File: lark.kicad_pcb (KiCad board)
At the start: 2 copper layers, 113 parts, among them CON1 SJ1-3523N, IC1 MS5611-01BA03, IC2 MS5611-01BA03, J1 SPI, J2 UART0, J3 I2C_0, J4 PWR_IN, J7 54602-908LF, J8 54602-908LF, J9 SOUND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

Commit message: Fitting layout into 57 mm instrument.
* board width is 51 mm at the moment
* split into two boards (sensor and main) which can be stacked with
  2.54 mm pinheaders.
* ESP32 was put to bottom with optional pcb antenna facing to front.
* added footprint for optional HCLAxxE on sensorboard
* added footprint for BMI088

* Is multiple GND pins for sensor board really a good idea (ground loops)?
* Does the +12V topology make sense (especially regarding the external
  IGC ports)?
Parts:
- removed C33, C34: 100n, Capacitor_SMD:C_0805_2012Metric_Pad1.15x1.40mm_HandSolder
- removed D3: 50V/3A, Diode_SMD:D_SOD-123
- removed L4: Ferrite_Bead, Inductor_SMD:L_0805_2012Metric_Pad1.15x1.40mm_HandSolder
- removed RV1: 3A/24V, Fuse:Fuse_2920_7451Metric_Pad2.10x5.45mm_HandSolder
- removed U8: BMX055, BMX055:BMX055
- added C25: 100n, Capacitor_SMD:C_0805_2012Metric_Pad1.15x1.40mm_HandSolder, F.Cu at (131.9, -34.1)
- added C26: 100n, Capacitor_SMD:C_0805_2012Metric_Pad1.15x1.40mm_HandSolder, F.Cu at (131.9, -36.0)
- added F3: 1.25A/16V, Fuse:Fuse_1812_4532Metric_Pad1.30x3.40mm_HandSolder, F.Cu at (36.0, 84.0)
- added J10: Conn_01x05-Connector_Generic, Connector_PinHeader_2.54mm:PinHeader_1x05_P2.54mm_Vertical, F.Cu at (-20.0, 94.0)
- added J11: Conn_01x20, Connector_PinSocket_2.54mm:PinSocket_1x20_P2.54mm_Vertical, F.Cu at (43.0, 52.0)
- added J12: Conn_01x20, Connector_PinSocket_2.54mm:PinSocket_1x20_P2.54mm_Vertical, F.Cu at (43.0, 97.0)
- added J5: Conn_01x05-Connector_Generic, Connector_PinHeader_2.54mm:PinHeader_1x05_P2.54mm_Vertical, F.Cu at (11.0, 52.0)
- added J6: Conn_01x05-Connector_Generic, Connector_PinHeader_2.54mm:PinHeader_1x05_P2.54mm_Vertical, F.Cu at (11.0, 97.0)
- added L3: Ferrite_Bead, Inductor_SMD:L_0805_2012Metric_Pad1.15x1.40mm_HandSolder, F.Cu at (-16.6, 104.4)
- added U6: BMI088, libs:LGA-16_handsolder, F.Cu at (84.0, 86.0)
- added U7: HCLAxxE, libs:HCLAxxE, F.Cu at (11.5, 90.5)
- C12, C9: value 1u -> 10u
- D4, D5: footprint Diode_SMD:D_SOD-123 -> Diode_SMD:D_SMA_Handsoldering
- F1: value 1.25A/16V -> 3A/24V
- L1: value 6A max. -> 10uH; footprint Inductor_SMD:L_1206_3216Metric_Pad1.42x1.75mm_HandSolder -> Inductor_SMD:L_Wuerth_WE-PD2-Typ-L
- MOD1: moved to B.Cu
- moved R26 226.6 mm to (10.5, 73.0), turned to 180 degrees
- moved R25 222.2 mm to (10.5, 60.5), turned to 180 degrees
- moved C23 190.2 mm to (-19.2, 104.6), turned to 270 degrees
- moved C22 181.6 mm to (-13.2, 104.6), turned to 270 degrees
- moved R38 176.9 mm to (10.5, 70.5), turned to 180 degrees
- moved R37 176.6 mm to (10.5, 63.0), turned to 180 degrees
- moved U4 176.0 mm to (-9.24, 104.6), turned to 270 degrees
- moved C21 169.4 mm to (-4.24, 104.6), turned to 270 degrees
- moved U5 146.6 mm to (1.00, 66.0), turned to 0 degrees
- moved C24 134.2 mm to (4.53, 57.0), turned to 0 degrees
- moved R17 107.2 mm to (10.5, 55.5), turned to 180 degrees
- moved R16 100.3 mm to (10.5, 68.0), turned to 180 degrees
- moved C36 96.8 mm to (-17.0, 71.0), turned to 0 degrees
- moved C16 96.3 mm to (54.0, 76.0), turned to 90 degrees
- moved C35 91.3 mm to (-16.5, 55.0), turned to 0 degrees
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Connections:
- net /Power/SENSPWR renamed /Sensors/SENSPWR
- net Net-(IC1-Pad7) renamed /Sensors/SDA0
- net Net-(IC1-Pad8) renamed /Sensors/SCK0
- net Net-(IC2-Pad7) renamed /Sensors/SDA1
- net Net-(IC2-Pad8) renamed /Sensors/SCK1
- net Net-(R26-Pad2) renamed /Sensors/SDA2
- net Net-(R38-Pad2) renamed /Sensors/SCK2
- C11 pad 1: +12V -> /Power/PWRIN
- C12 pad 1: +12V -> /Power/PWRIN
- C8 pad 1: Net-(C8-Pad1) -> +12V
- C9 pad 1: Net-(C8-Pad1) -> +12V
- D4 pad 1: Net-(D3-Pad2) -> +12V
- D5 pad 1: +12V -> /Power/PWRIN
- F1 pad 1: Net-(F1-Pad1) -> +12V
- F1 pad 2: +12V -> Net-(F1-Pad2)
- J4 pad 1: Net-(J4-Pad1) -> Net-(F1-Pad2)
- J7 pad 7: Net-(F1-Pad1) -> Net-(F2-Pad1)
- J7 pad 8: Net-(F1-Pad1) -> Net-(F2-Pad1)
- J8 pad 7: Net-(F2-Pad1) -> Net-(F3-Pad1)
- J8 pad 8: Net-(F2-Pad1) -> Net-(F3-Pad1)
- L1 pad 2: Net-(C8-Pad1) -> /Power/PWRIN
- R16 pad 2: Net-(R16-Pad2) -> /Sensors/SDA3
- R22 pad 1: +12V -> /Power/PWRIN
- R29 pad 2: Net-(R29-Pad2) -> /Sensors/SCK3
- U2 pad 1: +12V -> /Power/PWRIN
- U5 pad 15: Net-(R29-Pad2) -> /Sensors/SDA3
- U5 pad 16: Net-(R16-Pad2) -> /Sensors/SCK3
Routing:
- net /Sensors/SDA2: track 0.00 -> 46.5 mm, vias 0 -> 2
- net I2C0_SCK: track 44.7 -> 0.00 mm
- net I2C0_SDA: track 43.8 -> 0.00 mm
- net /Sensors/SCK2: track 0.00 -> 40.1 mm
- net SPID: track 8.72 -> 36.9 mm, vias 0 -> 1
- net Net-(R27-Pad1): track 0.00 -> 27.4 mm
- net Net-(R28-Pad1): track 0.00 -> 27.0 mm
- net /Sensors/SCK0: track 0.00 -> 26.7 mm, vias 0 -> 1
- net SPIQ: track 7.39 -> 33.7 mm, vias 0 -> 1
- net /Sensors/SDA0: track 0.00 -> 25.6 mm, vias 0 -> 1
- net /Sensors/SCK1: track 0.00 -> 25.4 mm, vias 0 -> 2
- net /Sensors/SDA1: track 0.00 -> 24.4 mm, vias 0 -> 2
- net SPICLK: track 7.14 -> 29.3 mm, vias 0 -> 1
- net BOOTM: track 15.1 -> 0.00 mm, vias 1 -> 0
- net SPICS0: track 14.2 -> 0.00 mm, vias 1 -> 0
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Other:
- board outline added: 150 x 51 mm

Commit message: Layout almost complete.
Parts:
- removed C26, C5, C6: 100n, Capacitor_SMD:C_0805_2012Metric_Pad1.15x1.40mm_HandSolder
- removed J12: Conn_01x20, Connector_PinSocket_2.54mm:PinSocket_1x20_P2.54mm_Vertical
- removed R10, R11, R12, R3, R4, R5, R6, R9: 10k, Resistor_SMD:R_0805_2012Metric_Pad1.15x1.40mm_HandSolder
- removed SW1: SW_ENTR, Button_Switch_THT:SW_Tactile_SPST_Angled_PTS645Vx83-2LFS
- removed SW2: SW_UP, Button_Switch_THT:SW_Tactile_SPST_Angled_PTS645Vx83-2LFS
- removed SW3: SW_DOWN, Button_Switch_THT:SW_Tactile_SPST_Angled_PTS645Vx83-2LFS
- removed SW4: SW_VARIO, TerminalBlock_Phoenix:TerminalBlock_Phoenix_PT-1,5-2-3.5-H_1x02_P3.50mm_Horizontal
- added H1: MountingHole, MountingHole:MountingHole_3.2mm_M3_DIN965, F.Cu at (191.4, 89.0)
- added H2: MountingHole, MountingHole:MountingHole_3.2mm_M3_DIN965, F.Cu at (141.4, 89.0)
- added H3: MountingHole, MountingHole:MountingHole_3.2mm_M3_DIN965, F.Cu at (191.4, 134.0)
- added H4: MountingHole, MountingHole:MountingHole_3.2mm_M3_DIN965, F.Cu at (141.4, 134.0)
- added IC3: BMP388, libs:LGA-10_2.0x2.0x0.75_handsolder, B.Cu at (68.6, 96.4)
- added IC4: BMP388, libs:LGA-10_2.0x2.0x0.75_handsolder, B.Cu at (68.6, 111.7)
- added TP1: dummy-mounting-footprint, libs:lark_sensor_mount, F.Cu at (67.4, 89.0)
- C3, C4: footprint Capacitor_SMD:C_0805_2012Metric_Pad1.15x1.40mm_HandSolder -> Capacitor_SMD:C_0603_1608Metric; moved to B.Cu
- J1: value SPI -> CONN1; footprint Connector_PinHeader_2.54mm:PinHeader_1x07_P2.54mm_Vertical -> Connector_PinHeader_2.54mm:PinHeader_1x15_P2.54mm_Vertical
- J11: value Conn_01x20 -> CONN1; footprint Connector_PinSocket_2.54mm:PinSocket_1x20_P2.54mm_Vertical -> Connector_PinHeader_2.54mm:PinHeader_1x15_P2.54mm_Vertical
- J2: value UART0 -> Conn_01x05-Connector_Generic; footprint Connector_PinHeader_2.54mm:PinHeader_1x06_P2.54mm_Vertical -> Connector_PinHeader_2.54mm:PinHeader_1x05_P2.54mm_Vertical
- J3: value I2C_0 -> Conn_01x05-Connector_Generic; footprint Connector_PinHeader_2.54mm:PinHeader_1x04_P2.54mm_Vertical -> Connector_PinHeader_2.54mm:PinHeader_1x05_P2.54mm_Vertical
- MOD1: moved to F.Cu
- moved C25 165.3 mm to (176.9, 125.0), turned to 90 degrees
- moved J11 164.3 mm to (185.4, 134.0), turned to 270 degrees
- moved C18 156.6 mm to (169.9, 129.5), turned to 270 degrees
- moved U3 156.1 mm to (173.9, 129.5), turned to 180 degrees
- moved C19 155.8 mm to (176.9, 129.5), turned to 270 degrees
- moved C20 148.3 mm to (174.4, 125.0)
- moved L2 147.6 mm to (171.9, 125.0), turned to 270 degrees
- moved C4 147.2 mm to (65.5, 111.7)
- moved J2 145.6 mm to (81.9, 134.0), turned to 90 degrees
- moved U1 145.5 mm to (158.2, 95.2), turned to 0 degrees
- moved C3 145.5 mm to (65.5, 96.4)
- moved C13 144.5 mm to (157.9, 92.5), turned to 0 degrees
- moved C15 143.3 mm to (162.7, 94.8), turned to 0 degrees
- moved C14 143.0 mm to (162.7, 92.5), turned to 0 degrees
- moved J1 123.5 mm to (185.4, 89.0), turned to 270 degrees
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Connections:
- C3 pad 1: BUT_ENTR -> GND
- C3 pad 2: GND -> /Sensors/SENSPWR
- C4 pad 1: BUT_UP -> GND
- C4 pad 2: GND -> /Sensors/SENSPWR
- J1 pad 1: +5V -> GND
- J1 pad 3: SPICLK -> +5V
- J1 pad 4: SPIQ -> BUT_ENTR
- J1 pad 5: SPID -> BUT_UP
- J1 pad 6: SPICS0 -> BUT_DOWN
- J1 pad 7: GND -> SW_VARIO
- J11 pad 1: Net-(J11-Pad1) -> GND
- J11 pad 11: Net-(J11-Pad11) -> EN
- J11 pad 12: Net-(J11-Pad12) -> BOOTM
- J11 pad 13: Net-(J11-Pad13) -> GND
- J11 pad 14: BUT_ENTR -> Net-(J11-Pad14)
- J11 pad 15: BUT_UP -> Net-(J11-Pad15)
- J11 pad 2: Net-(J11-Pad2) -> VDD
- J11 pad 3: Net-(J11-Pad3) -> +5V
- J11 pad 4: Net-(J11-Pad4) -> SPID
- J11 pad 5: Net-(J11-Pad5) -> SPIQ
- J11 pad 6: Net-(J11-Pad6) -> SPICLK
- J11 pad 7: Net-(J11-Pad7) -> SPICS0
- J11 pad 8: Net-(J11-Pad8) -> VDD
- J11 pad 9: Net-(J11-Pad9) -> U0RXD
- J2 pad 1: VDD -> +5V
- J2 pad 2: U0RXD -> Net-(J2-Pad2)
- J2 pad 3: Net-(J2-Pad3) -> I2C0_SDA
- J2 pad 4: EN -> I2C0_SCK
- J2 pad 5: BOOTM -> GND
- J3 pad 1: VDD -> +5V
- J3 pad 2: I2C0_SCK -> Net-(J3-Pad2)
- J3 pad 4: GND -> I2C0_SCK
- J5 pad 1: GND -> +5V
- J5 pad 2: I2C0_SCK -> Net-(J5-Pad2)
- J5 pad 4: Net-(J5-Pad4) -> I2C0_SCK
- J6 pad 1: +5V -> Net-(J6-Pad1)
- J6 pad 5: GND -> Net-(J6-Pad5)
- R23 pad 1: Net-(J2-Pad3) -> Net-(J11-Pad10)
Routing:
- net +5V: track 0.00 -> 259.5 mm, vias 0 -> 2
- net /Sensors/SENSPWR: track 4.37 -> 216.0 mm, vias 0 -> 2
- net VDD: track 0.00 -> 135.1 mm, vias 0 -> 5
- net I2C0_SCK: track 0.00 -> 134.4 mm, vias 0 -> 2
- net I2C0_SDA: track 0.00 -> 130.7 mm, vias 0 -> 2
- net Net-(J7-Pad3): track 0.00 -> 49.9 mm, vias 0 -> 2
- net EN: track 0.00 -> 49.4 mm, vias 0 -> 1
- net Net-(J8-Pad3): track 0.00 -> 49.0 mm, vias 0 -> 2
- net Net-(J8-Pad4): track 0.00 -> 47.1 mm, vias 0 -> 2
- net Net-(J7-Pad4): track 0.00 -> 41.1 mm, vias 0 -> 2
- net +12V: track 0.00 -> 38.1 mm
- net /Power/PWRIN: track 0.00 -> 33.3 mm
- net SW_VARIO: track 0.00 -> 32.9 mm, vias 0 -> 1
- net /Sensors/SCK3: track 6.21 -> 37.3 mm
- net BOOTM: track 0.00 -> 30.6 mm, vias 0 -> 2
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- added copper zone on B.Cu, net GND
- added copper zone on F.Cu, net GND
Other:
- board size 150 x 51 mm -> 137.5 x 51 mm
- net class Power2 removed

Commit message: even more finished
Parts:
- moved C1 46.8 mm to (157.4, 130.0)
- moved R2 44.5 mm to (159.4, 130.0)
- moved CON1 3.19 mm to (109.4, 128.5)
- moved J9 3.00 mm to (114.9, 133.0)
- moved C39 0.62 mm to (153.9, 128.0)
- moved F3 0.50 mm to (119.7, 104.0)
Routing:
- net EN: track 49.4 -> 54.6 mm
- net SPIQ: track 33.2 -> 36.9 mm
- net Net-(J9-Pad4): track 9.68 -> 13.3 mm
- net Net-(J9-Pad3): track 13.9 -> 17.5 mm
- net Net-(CON1-Pad1): track 25.4 -> 28.8 mm
- net Net-(CON1-Pad2): track 17.1 -> 19.9 mm
- net Net-(D2-Pad2): track 0.00 -> 1.95 mm
- net Net-(D1-Pad2): track 0.00 -> 1.95 mm
- net INT_ACC: track 36.7 -> 38.4 mm
- net VDD: track 135.1 -> 136.3 mm
- net SND_R: track 23.4 -> 24.3 mm
- net SND_L: track 27.6 -> 26.9 mm
- net I2C0_SCK: track 134.4 -> 133.8 mm
- net BUT_DOWN: track 16.5 -> 16.0 mm
- net GND: track 22.5 -> 22.9 mm, vias 33 -> 91
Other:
- outline, holes or cut-outs redrawn
- board text added: "+"
- board text added: "3V3"
- board text added: "5V"
- board text added: "BOOTM"
- board text added: "CLK"
- board text added: "CS0"
- board text added: "EN"
- board text added: "GND"
- board text added: "LED1"
- board text added: "LED2"
- board text added: "Lark Baro 2019-03.1"
- board text added: "Lark ESP32 2019-03.1"
- board text added: "Lark Vario"
- board text added: "MISO"
- board text added: "MOSI"
- board text added: "NC"
- board text added: "RX"
- board text added: "SCK"
- board text added: "SDA"
- board text added: "SW1"
- board text added: "SW2"
- board text added: "SW3"
- board text added: "SW4"
- board text added: "TX"

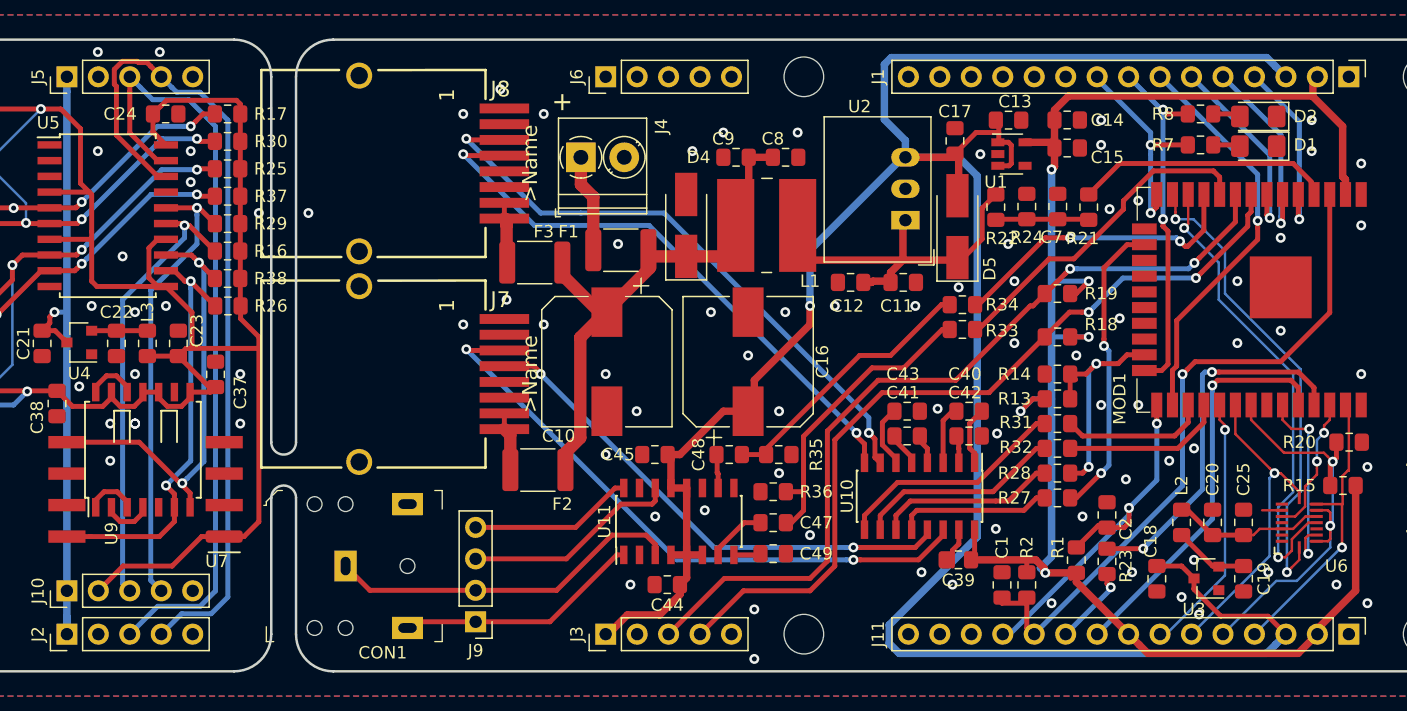
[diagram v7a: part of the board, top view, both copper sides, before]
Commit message: fix some vias
they were not shown correctly in the preview on aisler.net
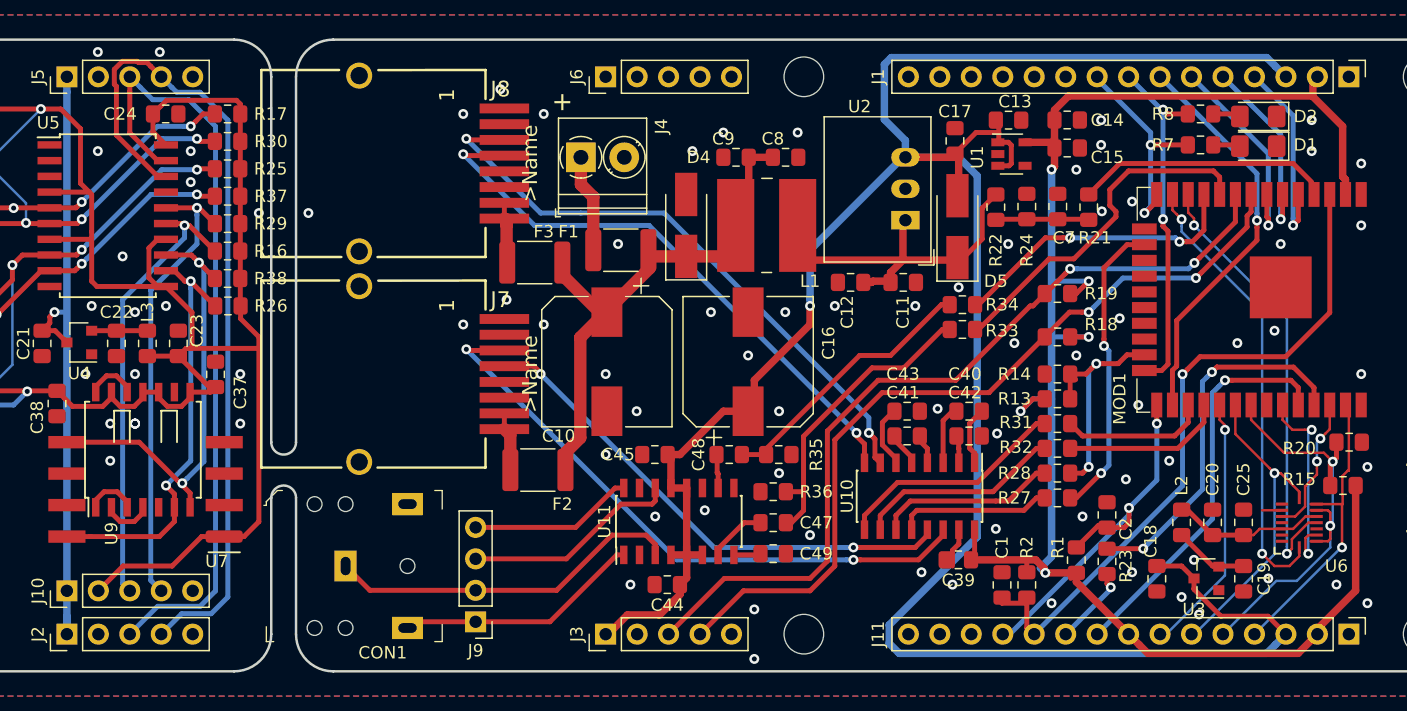
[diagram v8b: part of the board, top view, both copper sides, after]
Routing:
- net INT_GYR: track 37.9 -> 35.7 mm
- net INT_ACC: track 38.4 -> 36.4 mm
- net SND_L: track 26.9 -> 28.5 mm
- net LED1: track 17.6 -> 19.1 mm
- net BUT_DOWN: track 16.0 -> 17.1 mm
- net BUT_ENTR: track 15.0 -> 16.0 mm
- net BUT_UP: track 16.2 -> 15.5 mm
- net GND: vias 91 -> 87
